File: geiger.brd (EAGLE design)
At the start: 100 x 80 mm, 32 parts, among them IC1 AD8666N, X1 MINI-USB_SHIELD4P-85-32004-10X

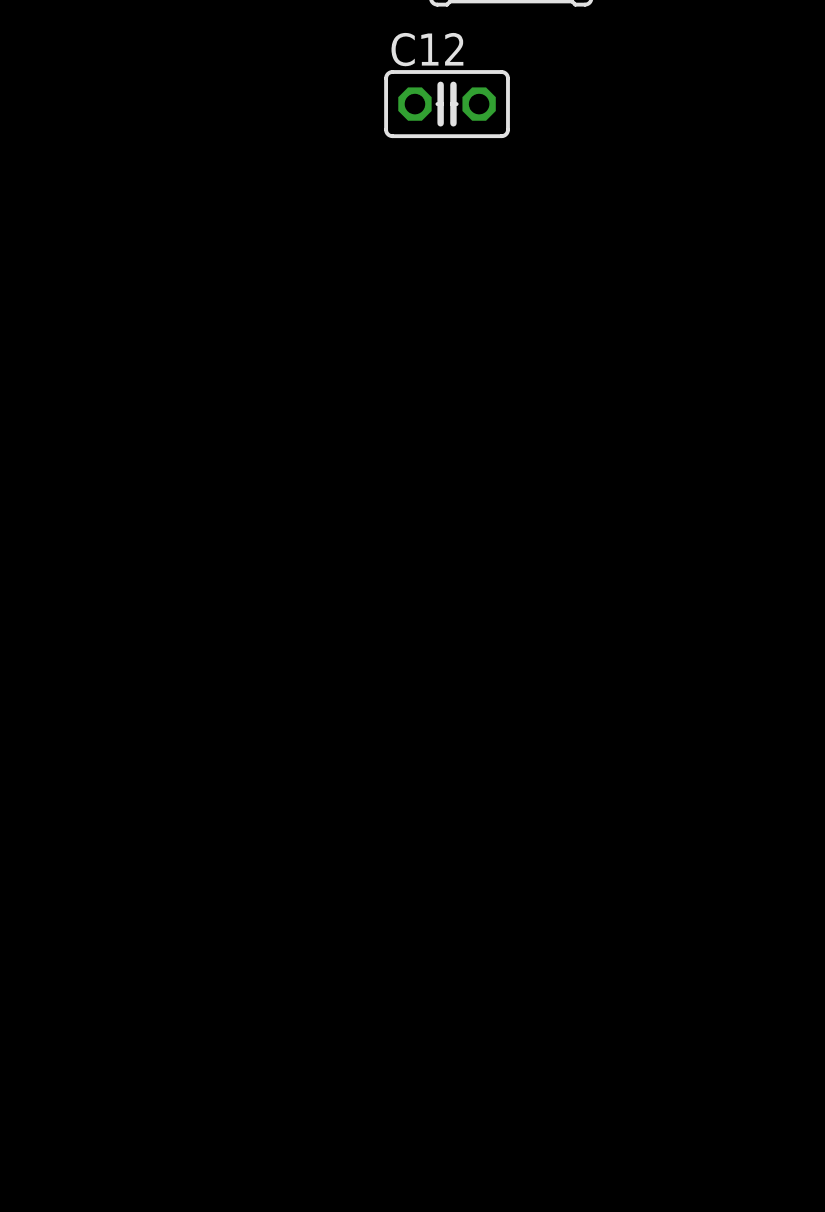
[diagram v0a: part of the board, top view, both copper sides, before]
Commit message: comperator added
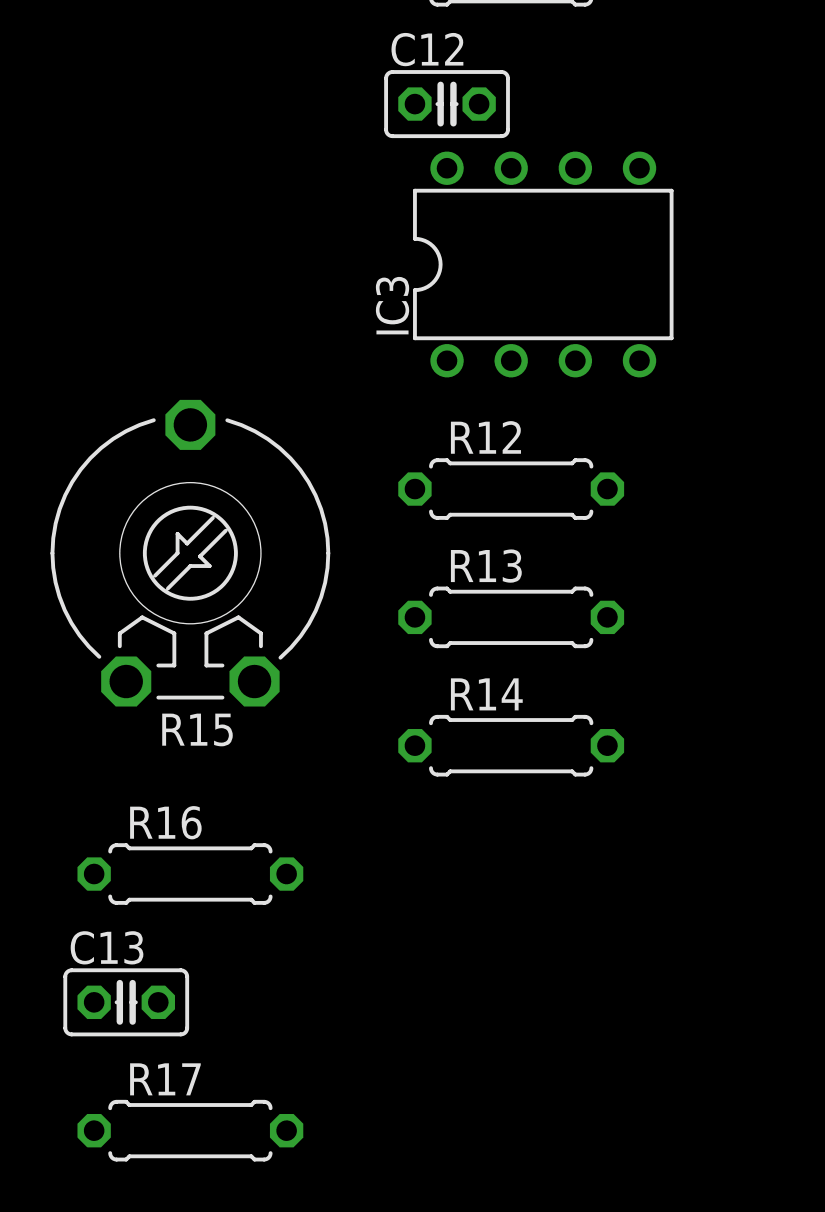
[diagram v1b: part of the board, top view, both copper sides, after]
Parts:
- added C13: (no value), resistor:C025-025X050
- added IC3: LM358N, linear:DIL08
- added R12: 3,3k, resistor:0207/7
- added R13, R14, R16, R17: 1k, resistor:0207/7
- added R15: (no value), pot:LI10
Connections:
- new net +3V3: C12.1, IC2.2, IC3.8, R10.1, R16.2, U$1.20
- new net N$17: IC3.2, R12.1, R13.2
- new net N$18: R15.E, R16.1
- new net N$19: C13.2, IC3.3, R15.S
- new net N$21: C13.1, IC3.1, R17.2
- new net N$22: IC3.5, R17.1
- net ANALOG_PULSE: now also R12.2
- net GND: now also IC3.4, R13.1, R14.1
- net N$16: now also R14.2, R15.A; no longer C12.1, IC2.2, R10.1, U$1.20
- net PULSE: now also IC3.6, IC3.7
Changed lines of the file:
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@@
 <element name="R11" library="resistor" package="0207/7" value="420" x="-30.48" y="-156.21"/>
 <element name="C12" library="resistor" package="C025-025X050" value="" x="-33.02" y="-161.29"/>
+<element name="IC3" library="linear" package="DIL08" value="LM358N" x="-29.21" y="-167.64"/>
+<element name="R12" library="resistor" package="0207/7" value="3,3k" x="-30.48" y="-176.53"/>
+<element name="R13" library="resistor" package="0207/7" value="1k" x="-30.48" y="-181.61"/>
+<element name="R14" library="resistor" package="0207/7" value="1k" x="-30.48" y="-186.69"/>
+<element name="R15" library="pot" package="LI10" value="" x="-43.18" y="-179.07"/>
+<element name="R16" library="resistor" package="0207/7" value="1k" x="-43.18" y="-191.77"/>
+<element name="C13" library="resistor" package="C025-025X050" value="" x="-45.72" y="-196.85"/>
+<element name="R17" library="resistor" package="0207/7" value="1k" x="-43.18" y="-201.93"/>
 </elements>
 <signals>
@@
 <contactref element="U$1" pad="10"/>
 <contactref element="C12" pad="2"/>
+<contactref element="IC3" pad="4"/>
+<contactref element="R13" pad="1"/>
+<contactref element="R14" pad="1"/>
+<wire x1="-34.29" y1="-181.61" x2="-34.29" y2="-186.69" width="0" layer="19" extent="1-1"/>
+<wire x1="-25.4" y1="-171.45" x2="-34.29" y2="-181.61" width="0" layer="19" extent="1-1"/>
+<wire x1="-31.75" y1="-161.29" x2="-25.4" y2="-171.45" width="0" layer="19" extent="1-1"/>
 <wire x1="-26.67" y1="-156.21" x2="-31.75" y2="-161.29" width="0" layer="19" extent="1-1"/>
 <wire x1="-22.69" y1="-125.71" x2="-26.67" y2="-156.21" width="0" layer="19" extent="1-1"/>
@@
 <contactref element="R7" pad="1"/>
 <contactref element="IC1" pad="7"/>
+<contactref element="R12" pad="2"/>
+<wire x1="-31.75" y1="-64.77" x2="-26.67" y2="-176.53" width="0" layer="19" extent="1-1"/>
 <wire x1="-34.29" y1="-59.69" x2="-31.75" y2="-64.77" width="0" layer="19" extent="1-1"/>
 <wire x1="-20.32" y1="10.16" x2="-34.29" y2="-59.69" width="0" layer="19" extent="1-1"/>
@@
 <signal name="PULSE">
 <contactref element="U$1" pad="11"/>
+<contactref element="IC3" pad="6"/>
+<contactref element="IC3" pad="7"/>
+<wire x1="-27.94" y1="-163.83" x2="-30.48" y2="-163.83" width="0" layer="19" extent="1-1"/>
+<wire x1="-8.89" y1="-87.63" x2="-27.94" y2="-163.83" width="0" layer="19" extent="1-1"/>
 </signal>
 <signal name="N$10">
@@
 <wire x1="-34.29" y1="-146.05" x2="-26.67" y2="-151.13" width="0" layer="19" extent="1-1"/>
 </signal>
-<signal name="N$16">
+<signal name="+3V3">
 <contactref element="IC2" pad="2"/>
 <contactref element="R10" pad="1"/>
 <contactref element="U$1" pad="20"/>
 <contactref element="C12" pad="1"/>
+<contactref element="IC3" pad="8"/>
+<contactref element="R16" pad="2"/>
+<wire x1="-33.02" y1="-163.83" x2="-39.37" y2="-191.77" width="0" layer="19" extent="1-1"/>
+<wire x1="-34.29" y1="-161.29" x2="-33.02" y2="-163.83" width="0" layer="19" extent="1-1"/>
 <wire x1="-34.29" y1="-151.13" x2="-34.29" y2="-161.29" width="0" layer="19" extent="1-1"/>
 <wire x1="-33.02" y1="-144.145" x2="-34.29" y2="-151.13" width="0" layer="19" extent="1-1"/>
 <wire x1="-31.75" y1="-87.63" x2="-33.02" y2="-144.145" width="0" layer="19" extent="1-1"/>
 </signal>
+<signal name="N$17">
+<contactref element="R12" pad="1"/>
+<contactref element="R13" pad="2"/>
+<contactref element="IC3" pad="2"/>
+<wire x1="-30.48" y1="-171.45" x2="-34.29" y2="-176.53" width="0" layer="19" extent="1-1"/>
+<wire x1="-26.67" y1="-181.61" x2="-34.29" y2="-176.53" width="0" layer="19" extent="1-1"/>
+</signal>
+<signal name="N$16">
+<contactref element="R14" pad="2"/>
+<contactref element="R15" pad="A"/>
+<wire x1="-26.67" y1="-186.69" x2="-45.72" y2="-184.15" width="0" layer="19" extent="1-1"/>
+</signal>
+<signal name="N$18">
+<contactref element="R16" pad="1"/>
+<contactref element="R15" pad="E"/>
+<wire x1="-40.64" y1="-184.15" x2="-46.99" y2="-191.77" width="0" layer="19" extent="1-1"/>
+</signal>
+<signal name="N$19">
+<contactref element="R15" pad="S"/>
+<contactref element="IC3" pad="3"/>
+<contactref element="C13" pad="2"/>
+<wire x1="-43.18" y1="-173.99" x2="-44.45" y2="-196.85" width="0" layer="19" extent="1-1"/>
+<wire x1="-27.94" y1="-171.45" x2="-43.18" y2="-173.99" width="0" layer="19" extent="1-1"/>
+</signal>
+<signal name="N$21">
+<contactref element="C13" pad="1"/>
+<contactref element="IC3" pad="1"/>
+<contactref element="R17" pad="2"/>
+<wire x1="-39.37" y1="-201.93" x2="-46.99" y2="-196.85" width="0" layer="19" extent="1-1"/>
+<wire x1="-33.02" y1="-171.45" x2="-46.99" y2="-196.85" width="0" layer="19" extent="1-1"/>
+</signal>
+<signal name="N$22">
+<contactref element="R17" pad="1"/>
+<contactref element="IC3" pad="5"/>
+<wire x1="-25.4" y1="-163.83" x2="-46.99" y2="-201.93" width="0" layer="19" extent="1-1"/>
+</signal>
 </signals>
